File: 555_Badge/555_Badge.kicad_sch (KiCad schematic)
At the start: 15 parts

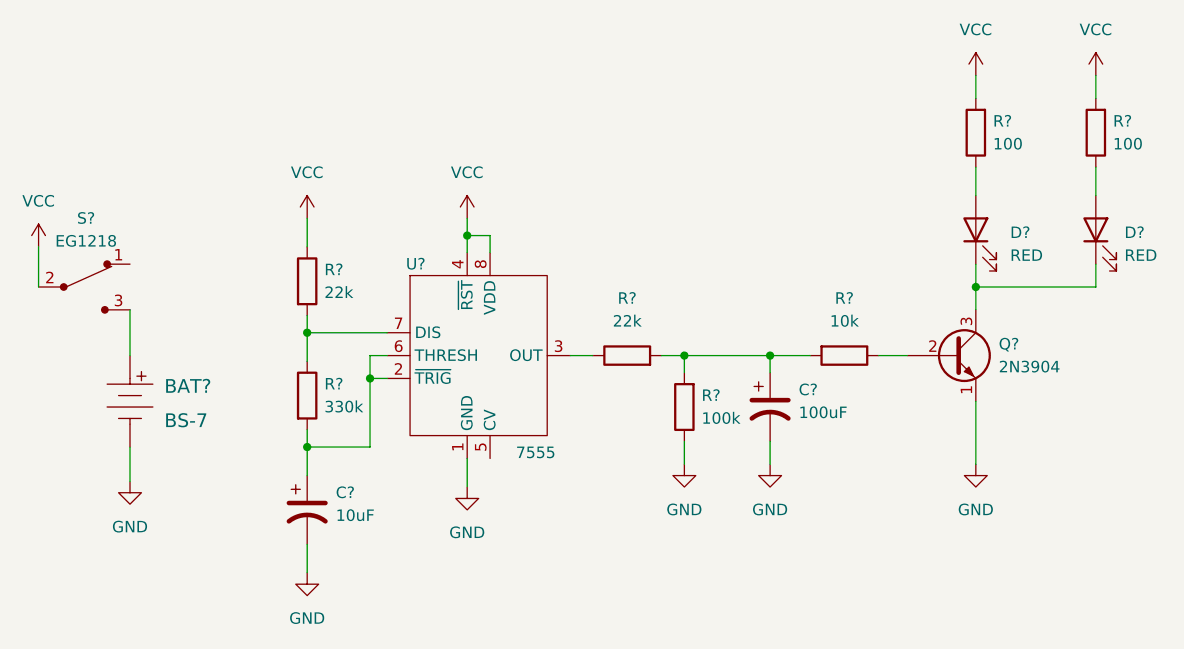
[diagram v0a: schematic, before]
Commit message: associated footprints and updated pcb from schematic
in kicad 6 you no longer need to generate netlist to use for pcb
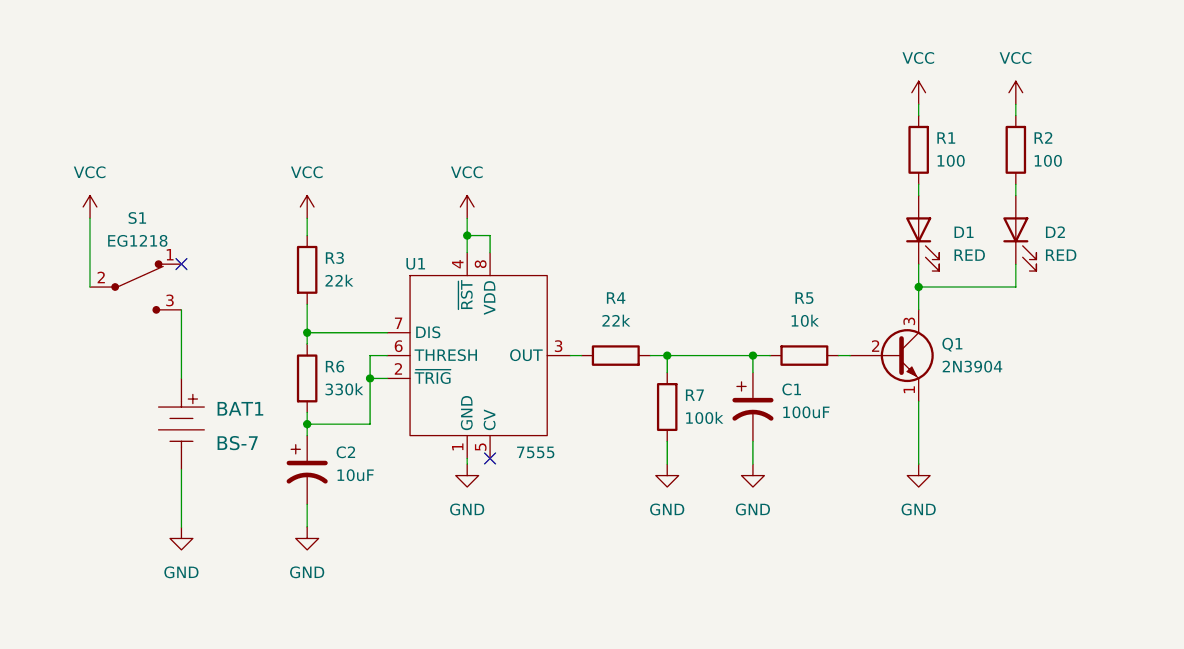
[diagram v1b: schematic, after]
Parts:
- C1: renamed from C?; footprint (none) -> Capacitor_THT:CP_Radial_D6.3mm_P2.50mm
- C2: renamed from C?; footprint (none) -> Capacitor_THT:CP_Radial_D5.0mm_P2.00mm
- D1, D2: renamed from D?; footprint (none) -> LED_THT:LED_D3.0mm
- Q1: renamed from Q?; footprint Package_TO_SOT_THT:TO-92_Inline -> digikey-footprints:TO-92-3
- R1, R2, R3, R4, R5, R6, R7: renamed from R?; footprint (none) -> Resistor_THT:R_Axial_DIN0207_L6.3mm_D2.5mm_P7.62mm_Horizontal
- U1: renamed from U?; footprint (none) -> 555_Badge:ICM7555-PDIP
- gave numbers to parts that had none: 2
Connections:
- no-connect marks 0 -> 2
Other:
- moved on the sheet: BAT1, C1, C2, D1, D2, Q1, R1, R2, R3, R4, R5, R6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
